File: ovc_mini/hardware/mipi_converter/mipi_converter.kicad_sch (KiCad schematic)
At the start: 8 parts, among them J1 Conn_01x28_Male, U1 MIPI_Custom_28Pin, U2 MIC23050, U3 PICAM_Expandable_Reversed

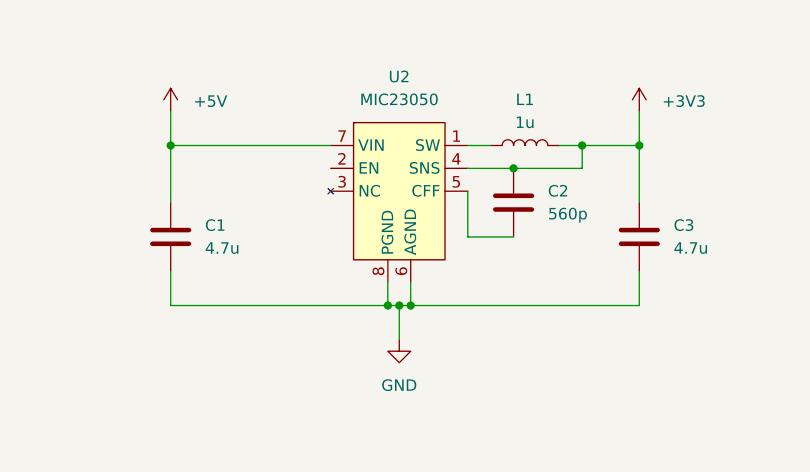
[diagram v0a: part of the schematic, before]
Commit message: Switched to hand-solderable LDO instead of switching regulator
Signed-off-by: Greg Balke <greg@openrobotics.org>
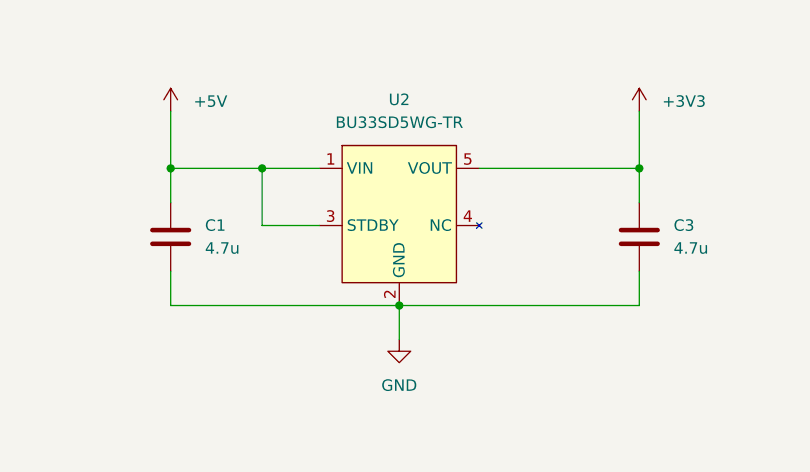
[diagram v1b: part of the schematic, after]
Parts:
- removed C2: 560p, Capacitor_SMD:C_0603_1608Metric, symbol Device:C
- removed L1: 1u, Inductor_SMD:L_0402_1005Metric_Pad0.77x0.64mm_HandSolder, symbol Device:L
- removed U2: MIC23050, Package_DFN_QFN:Micrel_MLF-8-1EP_2x2mm_P0.5mm_EP0.6x1.2mm, symbol DCDC_Converters:MIC23050
- added U2: BU33SD5WG-TR, digikey-footprints:SOT-753, symbol DCDC_Converters:BU33SD5WG-TR
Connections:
- net +3V3: now also U2.5 (VOUT)
- net +5V: now also U2.1 (VIN), U2.3 (STDBY)
- net GND: now also U2.2 (GND)
